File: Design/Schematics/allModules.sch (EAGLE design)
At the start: 92 parts, among them IC1 MAX7219CNG, IC2 MAX7219CNG, U1 328P, U2 328P, U3 328P

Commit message: Update Eagle version
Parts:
- removed C4: 20p, adafruit:C-US025-024X044
- removed GREEN_LED, RED_LED: (no value), adafruit:LED5MM
- removed LED46, LED47, LED48, LED51, LED52, LED53, LED54, LED55, LED56, LED59, LED60, LED61, LED62, LED63, LED64, LED67, LED68, LED69, LED70, LED71, LED72: (no value), Fidget Spinner Example:LEDCHIP-LED0805
- removed Q1: (no value), adafruit:CRYSTALHC18U-V
- added BIG_BTN: big, adafruit:SWITCH_PUSHBUTTONEVQ-PE
- added BIG_NUM: HD-H103, display-hp:HD-H103
- added BUTTON_LED, STATUS_LED, STATUS_LED1, STATUS_LED2, STATUS_LED3, STATUS_LED4, STRIP_LED: CLEAR, SparkFun-LED:LED-RGB-CCCLEAR
- added C5: 0.1u, adafruit:C-US025-024X044
- added CHAR1, CHAR2, CHAR3, CHAR4: (no value), adafruit:SWITCH_PUSHBUTTONEVQ-PE
- added DIS2, DIS5: HD-K121, display-hp:HD-K121
- added IC3: MAX7219CNG, maxim:MAX7219CNG
- added JP1, JP10, JP11, JP12, JP2, JP3, JP4, JP5, JP6, JP7, JP8, JP9: (no value), adafruit:PINHD-1X1
- added LED1, LED11, LED12, LED13, LED14, LED15, LED16, LED17, LED18, LED19, LED2, LED20, LED21, LED22, LED23, LED24, LED25, LED26, LED3, LED33, LED34, LED4, LED41, LED42, LED5: green, adafruit:LED5MM
- added R22, R23, R24, R25, R26, R27: 1k, adafruit:FLIPFLOP-RES
- added R28, R29, R30, R31, R33, R34, R35, R36, R37, R38: 330, adafruit:R-US_0309/12
- added R32, R39, R40, R41: 10k, adafruit:R-US_0309/12
- added RSET, RSET1: 24.5k, BeagleBone_Black_Wireless:R-US_0204/7
- added U4, U5, U6: 328P, SparkFun-IC-Microcontroller:ATMEGA328P_PDIP
- C3: value 20p -> 0.1u
- CLEAR, LED6: value (none) -> green
- CLOCK_1, CLOCK_2, STRIKE_1, STRIKE_2: value (none) -> red
- LED10, LED7, LED8, LED9, SW1, SW2, SW3, SW4: value (none) -> arcade_btn
- LED27, LED28, LED29, LED30, LED31, LED32, LED35, LED36, LED37, LED38, LED39, LED40, LED43, LED44, LED45: value (none) -> green; device Fidget Spinner Example:LEDCHIP-LED0805 -> adafruit:LED5MM
- R1, R2, R3, R4, R5, R6, R7, R8, R9: value (none) -> 330; device adafruit:FLIPFLOP-RES -> adafruit:R-US_0309/12
- R10: value (none) -> 10k; device adafruit:FLIPFLOP-RES -> adafruit:R-US_0309/12
- R11, R12, R13, R14: value (none) -> 10k; device adafruit:R-US_0207/12 -> adafruit:R-US_0309/12
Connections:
- new net GND2: R14.2
- new net N$100: STATUS_LED4.RED, U6.PB5(SCK)
- new net N$101: DIS5.CA1, IC3.DIG3
- new net N$102: DIS5.CA2, IC3.DIG2
- new net N$103: DIS2.CA2, IC3.DIG1
- new net N$104: DIS2.CA1, IC3.DIG0
- new net N$105: LED1.C, R37.2
- new net N$106: LED2.C, R36.2
- new net N$107: IC3.CLK, U6.PB1(OC1A)
- new net N$108: IC3.DIN, U6.PB3(MOSI/OC2)
- new net N$109: IC3.LOAD, U6.PB2(SS/OC1B)
- new net N$110: C3.1, IC3.ISET, RSET1.1
- new net N$111: LED3.C, R35.2
- new net N$112: LED4.C, R34.2
- new net N$113: LED5.C, R38.2
- new net N$114: R34.1, R35.1, R36.1, R37.1, R38.1, U6.PC4(ADC4/SDA), U6.PC5(ADC5/SCL), U6.PD2(INT0), U6.PD3(INT1), U6.PD4(XCK/T0)
- new net N$117: BIG_NUM.CC, BIG_NUM.CC@1, IC3.DIG4
- new net N$118: CHAR4.P$2, R41.2, U6.PD5(T1)
- new net N$119: CHAR3.P$2, R40.2, U6.PD6(AIN0)
- new net N$120: CHAR2.P$2, R39.2, U6.PD7(AIN1)
- new net N$121: CHAR1.P$2, U6.PB0(ICP)
- new net N$71: STATUS_LED1.GRN, U2.PD2(INT0)
- new net N$72: R21.1, STATUS_LED1.C
- new net N$73: C5.1, IC1.ISET, RSET.1
- new net N$74: JP5.1, R23.1, U4.PC4(ADC4/SDA)
- new net N$75: STATUS_LED2.GRN, U4.PD3(INT1)
- new net N$76: STATUS_LED2.RED, U4.PD4(XCK/T0)
- new net N$77: R29.1, STATUS_LED3.C
- new net N$78: STATUS_LED3.GRN, U5.PD2(INT0)
- new net N$79: STATUS_LED3.RED, U5.PD3(INT1)
- new net N$80: BUTTON_LED.C, R30.1
- new net N$81: BUTTON_LED.GRN, U5.PD4(XCK/T0)
- new net N$82: BUTTON_LED.BLU, U5.PD5(T1)
- new net N$83: R31.1, STRIP_LED.C
- new net N$84: BUTTON_LED.RED, U5.PD6(AIN0)
- new net N$85: STRIP_LED.GRN, U5.PD7(AIN1)
- new net N$86: STRIP_LED.BLU, U5.PB0(ICP)
- new net N$87: STRIP_LED.RED, U5.PB1(OC1A)
- new net N$88: BIG_BTN.P$1, R32.1, U5.PB2(SS/OC1B)
- new net N$90: R33.1, STATUS_LED4.C
- new net N$91: BIG_NUM.A, DIS2.A1, DIS2.A2, DIS5.A1, DIS5.A2, IC3.SEGA
- new net N$92: BIG_NUM.B, DIS2.B1, DIS2.B2, DIS5.B1, DIS5.B2, IC3.SEGB
- new net N$93: BIG_NUM.C, DIS2.C1, DIS2.C2, DIS5.C1, DIS5.C2, IC3.SEGC
- new net N$94: BIG_NUM.D, DIS2.D1, DIS2.D2, DIS5.D1, DIS5.D2, IC3.SEGD
- new net N$95: BIG_NUM.E, DIS2.E1, DIS2.E2, DIS5.E1, DIS5.E2, IC3.SEGE
- new net N$96: BIG_NUM.F, DIS2.F1, DIS2.F2, DIS5.F1, DIS5.F2, IC3.SEGF
- new net N$97: BIG_NUM.G, DIS2.G1, DIS2.G2, DIS5.G1, DIS5.G2, IC3.SEGG
- new net N$98: BIG_NUM.DP, DIS2.DP1, DIS2.DP2, DIS5.DP1, DIS5.DP2, IC3.SEGDP
- new net N$99: STATUS_LED4.GRN, U6.PB4(MISO)
- new net VCC1: R10.1
- new net VCC2: LED6.A
- net GND: now also C5.2, CHAR1.P$1, CHAR2.P$1, CHAR3.P$1, CHAR4.P$1, IC1.GND@1, IC1.GND@2, IC3.GND@1, IC3.GND@2, R1.2, R2.2, R22.2, R23.2, R24.2, R25.2, R26.2, R27.2, R28.2, R29.2, R3.2, R30.2, R31.2, R32.2, R33.2, R4.2, R5.2, SV1.1, U1.GND@2, U4.GND@1, U4.GND@2, U5.GND@2, U6.GND@2; no longer C4.2
- net N$20: now also JP6.1, R22.1, U4.PC5(ADC5/SCL); no longer IC1.GND@2, SV1.1, U1.GND@2
- net N$21: now also R28.1, STATUS_LED2.C; no longer IC1.VCC, SV1.4, U1.VCC
- net N$22: now also R4.1; no longer R5.2
- net N$23: now also R3.1; no longer R4.2
- net N$24: now also R2.1; no longer R3.2
- net N$25: now also R1.1; no longer R2.2
- net N$26: now also R5.1; no longer R1.2
- net N$27: now also JP1.1, R27.1, U4.PC0(ADC0); no longer R1.1, R2.1, R3.1, R4.1, R5.1, U1.GND@1
- net N$34: no longer R14.2
- net N$35: now also R11.1; no longer R13.1
- net N$36: now also LED20.A, LED21.A, LED22.A, LED23.A, LED24.A, LED25.A; no longer LED67.A, LED68.A, LED69.A, LED70.A, LED71.A, LED72.A
- net N$37: now also JP2.1, R26.1, U4.PC1(ADC1); no longer LED10.A, LED6.A, LED7.A, LED8.A, LED9.A, R11.1, R12.1, R13.2, R14.1, U2.VCC
- net N$38: now also R12.1; no longer R12.2
- net N$39: now also R13.1; no longer R11.2
- net N$40: now also LED19.A, LED26.A, LED36.A, LED37.A, LED38.A, LED39.A; no longer LED59.A, LED60.A, LED61.A, LED62.A, LED63.A, LED64.A
- net N$41: now also LED18.A, LED27.A, LED35.A, LED40.A, LED44.A, LED45.A; no longer LED51.A, LED52.A, LED53.A, LED54.A, LED55.A, LED56.A
- net N$42: now also LED17.A, LED28.A, LED34.A, LED41.A, LED42.A; no longer LED44.A, LED45.A, LED46.A, LED47.A, LED48.A
- net N$43: now also R6.2, U2.PB1(OC1A); no longer LED6.C, R10.2
- net N$44: now also R8.1; no longer R9.2
- net N$45: now also R7.1; no longer R8.2
- net N$46: now also R6.1; no longer R7.2
- net N$47: now also R9.1; no longer R6.2
- net N$48: now also R7.2, R8.2, R9.2; no longer R10.1, R6.1, R7.1, R8.1, R9.1, U2.PB1(OC1A), U2.PB4(MISO)
- net N$49: now also LED25.C, LED26.C, LED28.C, LED29.C, LED6.C; no longer LED35.C, LED43.C, LED51.C, LED59.C, LED67.C
- net N$50: now also LED11.A, LED12.A, LED13.A, LED14.A, LED15.A; no longer LED27.A, LED28.A, LED29.A, LED30.A, LED31.A, LED32.A
- net N$51: now also JP3.1, R25.1, U4.PC2(ADC2); no longer C4.1, Q1.2, U3.PB6(XTAL1/TOSC1)
- net N$52: now also LED16.A, LED29.A, LED30.A, LED31.A, LED32.A, LED33.A; no longer LED35.A, LED36.A, LED37.A, LED38.A, LED39.A, LED40.A
- net N$54: now also LED11.C, LED24.C, LED30.C, LED39.C, LED40.C, LED41.C; no longer LED28.C, LED36.C, LED44.C, LED52.C, LED60.C, LED68.C
- net N$55: now also LED12.C, LED23.C, LED31.C, LED38.C, LED42.C; no longer LED29.C, LED37.C, LED53.C, LED61.C, LED69.C
- net N$56: now also LED13.C, LED22.C, LED32.C, LED37.C, LED43.C, LED44.C; no longer LED30.C, LED38.C, LED46.C, LED54.C, LED62.C, LED70.C
- net N$57: now also LED14.C, LED21.C, LED33.C, LED34.C, LED35.C, LED36.C; no longer LED31.C, LED39.C, LED47.C, LED55.C, LED63.C, LED71.C
- net N$58: now also LED15.C, LED16.C, LED17.C, LED18.C, LED19.C, LED20.C; no longer LED32.C, LED40.C, LED48.C, LED56.C, LED64.C, LED72.C
- net N$66: now also JP4.1, R24.1, U4.PC3(ADC3); no longer C3.1, Q1.1, U3.PB7(XTAL2/TOSC2)
- net N$67: now also STATUS_LED.RED; no longer RED_LED.A
- net N$68: now also STATUS_LED.GRN; no longer GREEN_LED.A
- net N$69: now also STATUS_LED.C; no longer GREEN_LED.C
- net N$70: now also STATUS_LED1.RED, U2.PD3(INT1); no longer R21.1, RED_LED.C
- net VCC: now also BIG_BTN.P$2, IC1.VCC, IC3.VCC, JP10.1, JP11.1, JP12.1, JP7.1, JP8.1, JP9.1, LED1.A, LED10.A, LED2.A, LED3.A, LED4.A, LED5.A, LED7.A, LED8.A, LED9.A, R10.2, R11.2, R12.2, R13.2, R14.1, R39.1, R40.1, R41.1, RSET.2, RSET1.2, SV1.4, U1.AVCC, U1.VCC, U2.AVCC, U2.VCC, U4.AVCC, U4.VCC, U5.AVCC, U5.VCC, U6.AVCC, U6.VCC

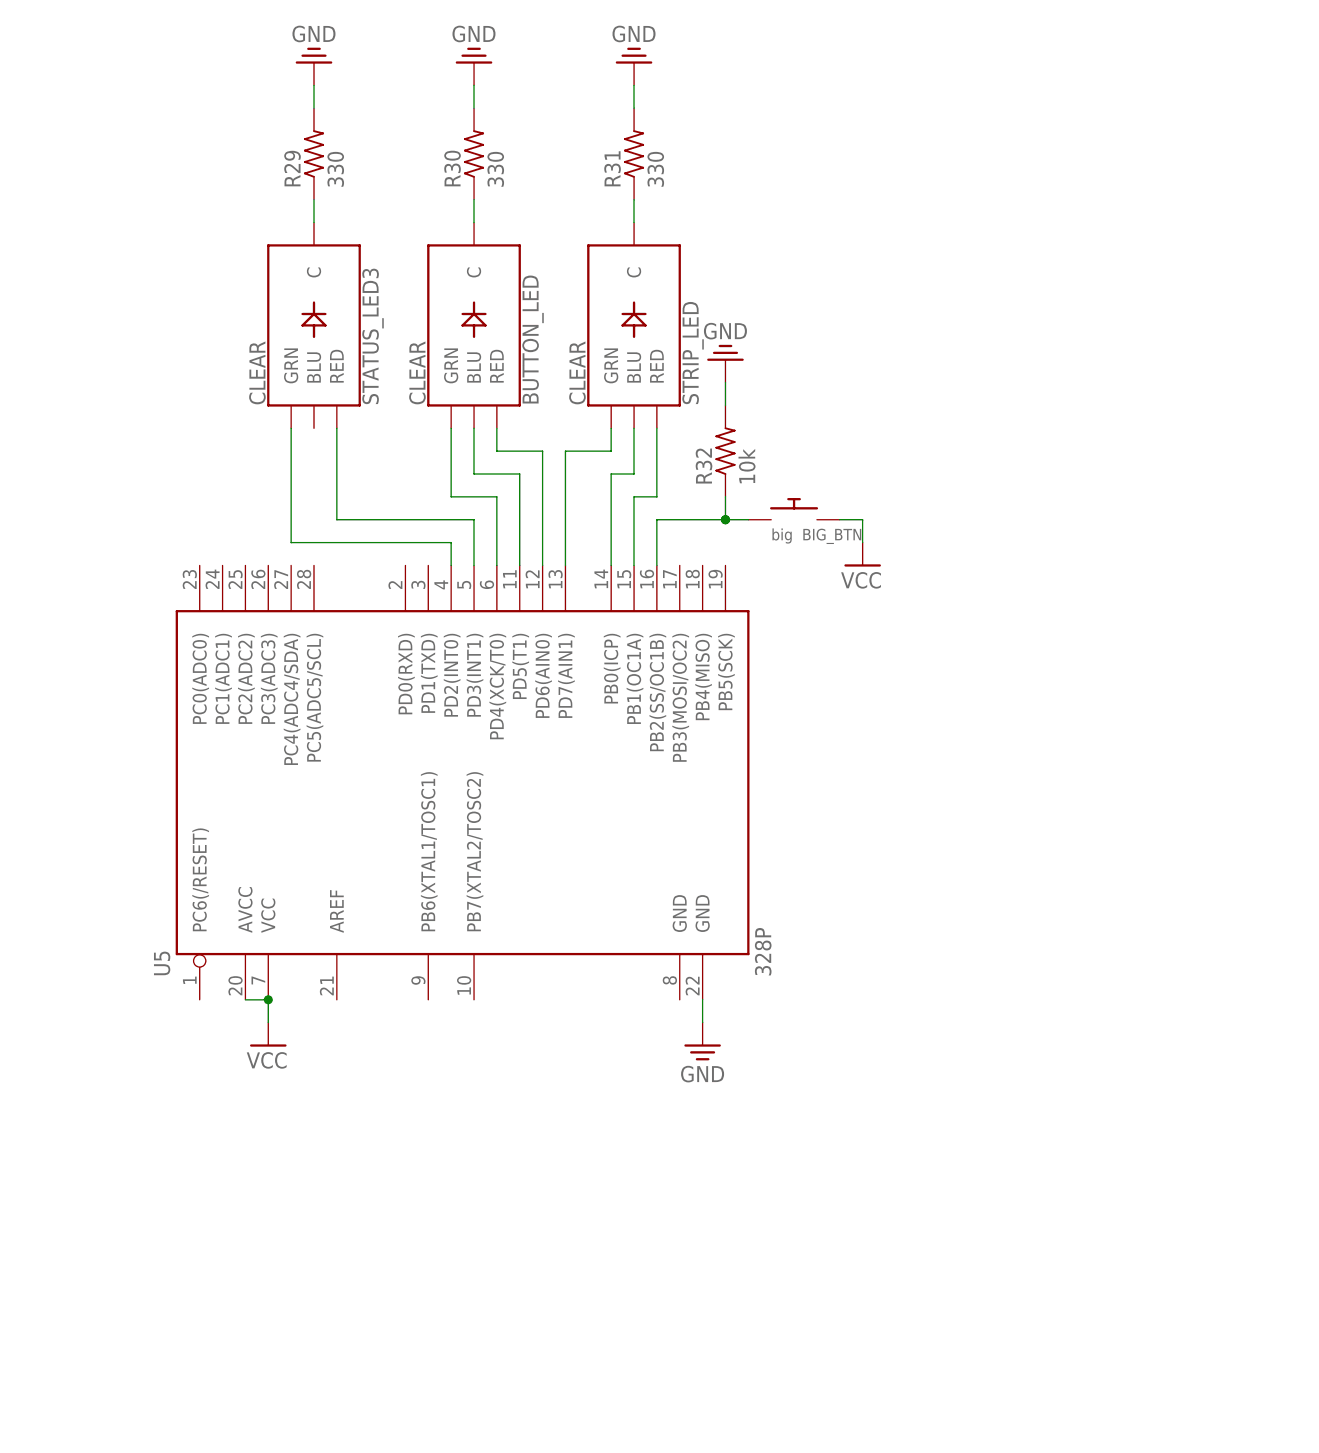
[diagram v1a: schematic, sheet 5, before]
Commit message: Made code match schematics
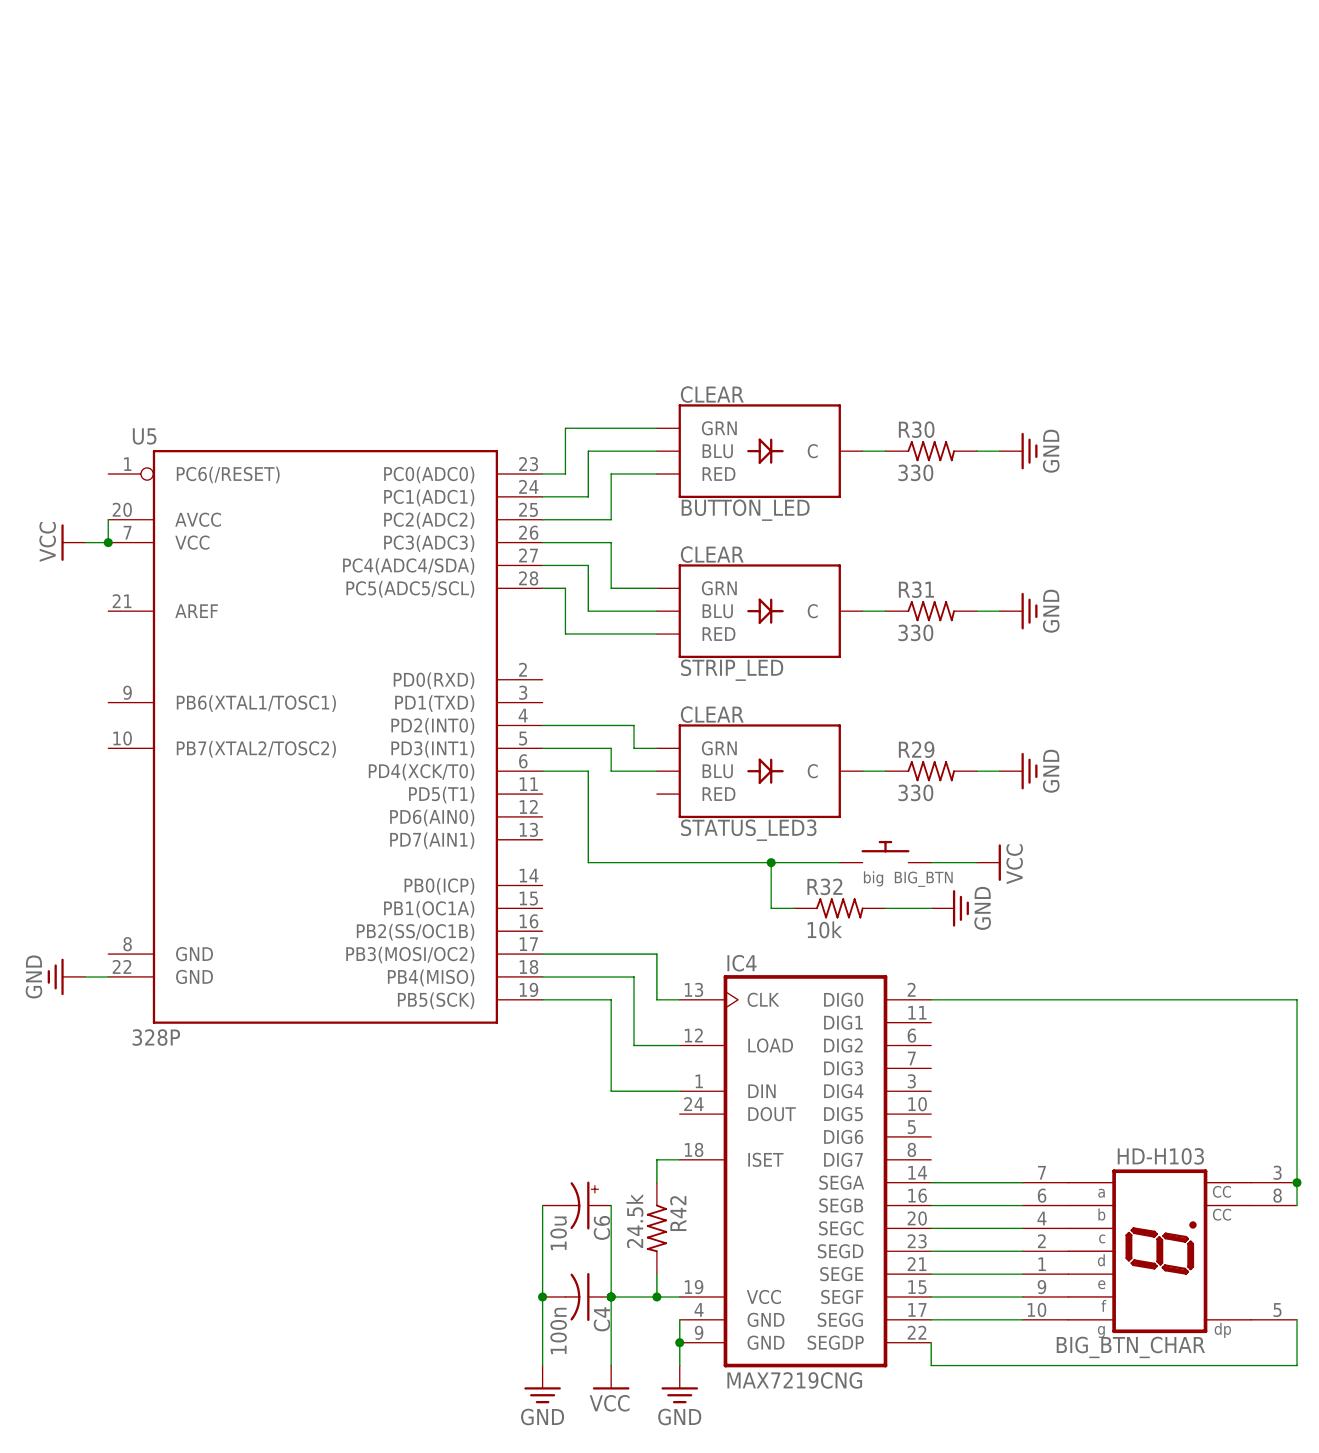
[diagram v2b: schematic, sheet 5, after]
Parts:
- removed LED10, LED7, LED8, LED9: arcade_btn, adafruit:LED5MM
- added BIG_BTN_CHAR: HD-H103, display-hp:HD-H103
- added BLUE, GREEN, RED, YELLOW: arcade_btn, adafruit:LED5MM
- added BUZZER: EB2209A, buzzer:EB2209A
- added C4: 100n, adafruit:C-US025-024X044
- added C6: 10u, adafruit:CPOL-US085CS-1AR
- added IC4: MAX7219CNG, maxim:MAX7219CNG
- added R42: 24.5k, adafruit:R-US_0309/12
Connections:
- removed net GND2: R14.2
- removed net N$107: IC3.CLK, U6.PB1(OC1A)
- removed net N$109: IC3.LOAD, U6.PB2(SS/OC1B)
- removed net VCC1: R10.1
- new net N$115: BUZZER.+, U1.PD3(INT1)
- new net N$116: R9.2, U2.PB2(SS/OC1B)
- new net N$122: IC4.ISET, R42.1
- new net N$123: IC4.DIN, U5.PB5(SCK)
- new net N$125: IC4.LOAD, U5.PB4(MISO)
- new net N$126: BIG_BTN_CHAR.D, IC4.SEGD
- new net N$127: STRIP_LED.BLU, U5.PC4(ADC4/SDA)
- new net N$128: STRIP_LED.RED, U5.PC5(ADC5/SCL)
- new net N$129: BIG_BTN_CHAR.E, IC4.SEGE
- new net N$130: BIG_BTN_CHAR.F, IC4.SEGF
- new net N$131: BIG_BTN_CHAR.G, IC4.SEGG
- new net N$132: BIG_BTN_CHAR.DP, IC4.SEGDP
- new net N$133: BIG_BTN_CHAR.CC, BIG_BTN_CHAR.CC@1, IC4.DIG0
- new net N$134: R34.1, U6.PC3(ADC3)
- new net N$135: IC3.LOAD, U6.PB3(MOSI/OC2)
- new net N$136: CHAR2.P$2, R40.2, U6.PD3(INT1)
- new net N$137: IC3.DIN, U6.PB4(MISO)
- new net N$89: BIG_BTN_CHAR.C, IC4.SEGC
- net GND: now also BUZZER.-, C4.2, C6.-, IC4.GND@1, IC4.GND@2
- net N$100: now also U6.PD7(AIN1); no longer U6.PB5(SCK)
- net N$108: now also IC4.CLK, U5.PB3(MOSI/OC2); no longer IC3.DIN, U6.PB3(MOSI/OC2)
- net N$114: now also U6.PC0(ADC0), U6.PC1(ADC1), U6.PC2(ADC2); no longer R34.1, U6.PC5(ADC5/SCL), U6.PD2(INT0), U6.PD3(INT1), U6.PD4(XCK/T0)
- net N$118: now also CHAR1.P$2, U6.PD2(INT0); no longer CHAR4.P$2, U6.PD5(T1)
- net N$119: now also IC3.CLK, U6.PB2(SS/OC1B); no longer CHAR3.P$2, R40.2, U6.PD6(AIN0)
- net N$120: now also CHAR3.P$2, U6.PD4(XCK/T0); no longer CHAR2.P$2, U6.PD7(AIN1)
- net N$121: now also CHAR4.P$2, R14.2, U6.PD5(T1); no longer CHAR1.P$2, U6.PB0(ICP)
- net N$17: now also U1.PB2(SS/OC1B); no longer U1.PB3(MOSI/OC2)
- net N$19: now also U1.PB3(MOSI/OC2); no longer U1.PB2(SS/OC1B)
- net N$22: now also STRIKE_1.C; no longer STRIKE_2.C
- net N$23: now also STRIKE_2.C; no longer STRIKE_1.C
- net N$28: now also STRIKE_1.A, U1.PD4(XCK/T0); no longer STRIKE_2.A, U1.PD6(AIN0)
- net N$29: now also STRIKE_2.A, U1.PD5(T1); no longer STRIKE_1.A, U1.PD7(AIN1)
- net N$30: now also U1.PD6(AIN0); no longer U1.PB0(ICP)
- net N$31: now also U1.PD7(AIN1); no longer U1.PB1(OC1A)
- net N$34: now also R10.1
- net N$43: now also U2.PB3(MOSI/OC2); no longer U2.PB1(OC1A)
- net N$44: now also BLUE.C; no longer LED7.C
- net N$45: now also GREEN.C; no longer LED8.C
- net N$46: now also YELLOW.C; no longer LED9.C
- net N$47: now also RED.C; no longer LED10.C
- net N$48: now also U2.PB4(MISO), U2.PB5(SCK); no longer R9.2, U2.PB0(ICP), U2.PB2(SS/OC1B), U2.PB3(MOSI/OC2)
- net N$53: now also U3.PD7(AIN1); no longer U3.PB1(OC1A)
- net N$59: now also U3.PD6(AIN0); no longer U3.PB0(ICP)
- net N$60: now also U3.PD5(T1); no longer U3.PD7(AIN1)
- net N$62: now also U3.PD4(XCK/T0); no longer U3.PD6(AIN0)
- net N$64: now also U3.PB2(SS/OC1B); no longer U3.PB3(MOSI/OC2)
- net N$65: now also U3.PB3(MOSI/OC2); no longer U3.PB2(SS/OC1B)
- net N$67: now also U3.PD3(INT1); no longer U3.PD4(XCK/T0)
- net N$68: now also U3.PD2(INT0); no longer U3.PD3(INT1)
- net N$75: now also U4.PD2(INT0); no longer U4.PD3(INT1)
- net N$76: now also U4.PD3(INT1); no longer U4.PD4(XCK/T0)
- net N$79: now also STATUS_LED3.BLU; no longer STATUS_LED3.RED
- net N$81: now also BIG_BTN.P$1, R32.1; no longer BUTTON_LED.GRN
- net N$82: now also BIG_BTN_CHAR.A, IC4.SEGA; no longer BUTTON_LED.BLU, U5.PD5(T1)
- net N$84: now also BIG_BTN_CHAR.B, IC4.SEGB; no longer BUTTON_LED.RED, U5.PD6(AIN0)
- net N$85: now also BUTTON_LED.GRN, U5.PC0(ADC0); no longer STRIP_LED.GRN, U5.PD7(AIN1)
- net N$86: now also BUTTON_LED.BLU, U5.PC1(ADC1); no longer STRIP_LED.BLU, U5.PB0(ICP)
- net N$87: now also BUTTON_LED.RED, U5.PC2(ADC2); no longer STRIP_LED.RED, U5.PB1(OC1A)
- net N$88: now also STRIP_LED.GRN, U5.PC3(ADC3); no longer BIG_BTN.P$1, R32.1, U5.PB2(SS/OC1B)
- net N$99: now also U6.PD6(AIN0); no longer U6.PB4(MISO)
- net VCC: now also BLUE.A, C4.1, C6.+, GREEN.A, IC4.VCC, R42.2, RED.A, YELLOW.A; no longer LED10.A, LED7.A, LED8.A, LED9.A
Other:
- moved on the sheet: BIG_BTN, BUTTON_LED, CHAR1, CHAR2, CHAR3, CHAR4, R10, R11, R12, R13, R14, R29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
